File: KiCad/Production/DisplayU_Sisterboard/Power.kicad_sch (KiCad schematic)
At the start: 31 parts

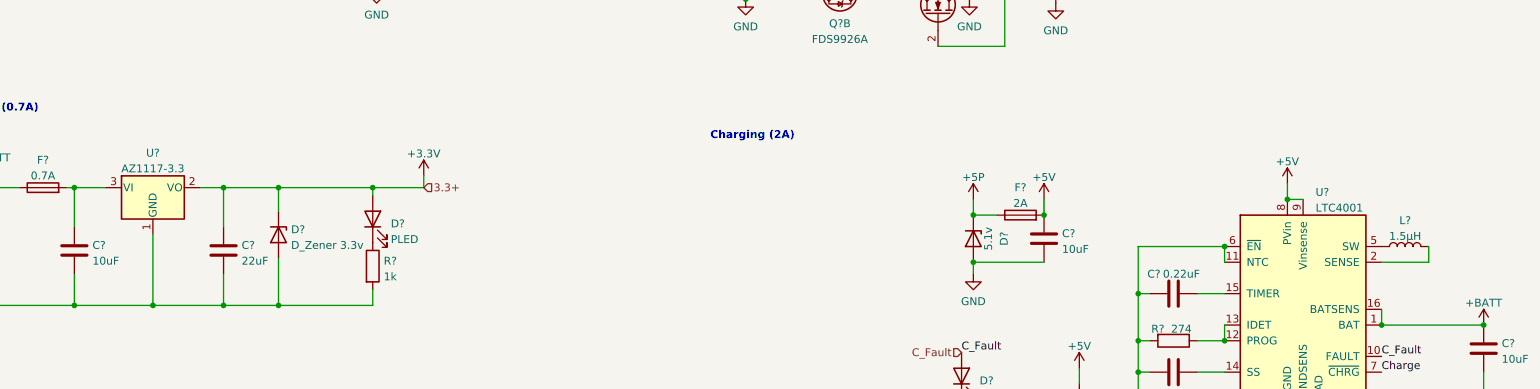
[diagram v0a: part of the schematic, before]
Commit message: Microcontroller Choice
Nordic nRF52820
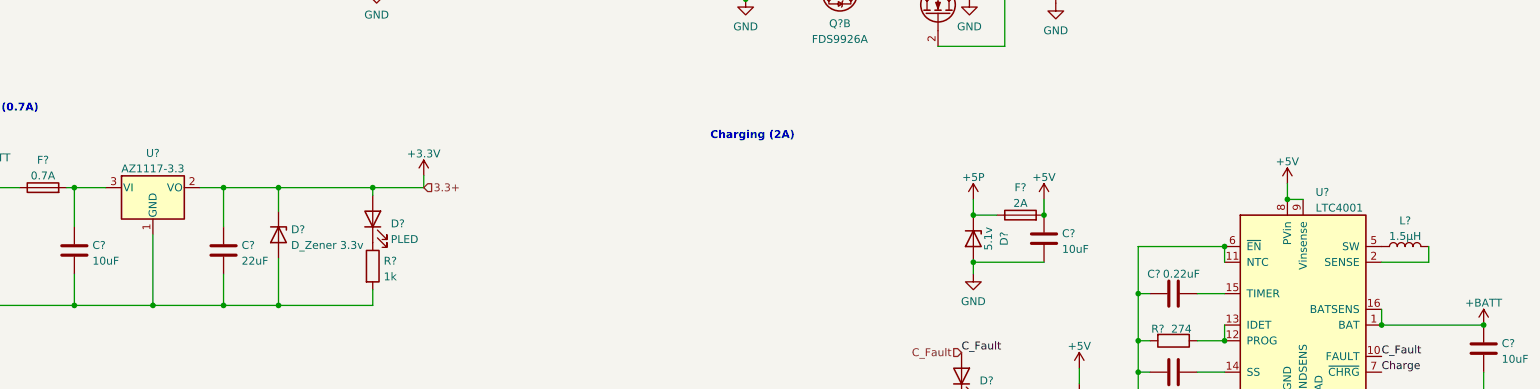
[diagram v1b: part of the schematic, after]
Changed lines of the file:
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@@
       (project "DisplayU_Sisterboard"
         (path "/19c7c935-33c8-4c59-9a5d-d605e15c31a3/bc90aa39-2744-4a84-88b0-6b5f6472e99d"
-          (reference "U6") (unit 1)
+          (reference "U4") (unit 1)
         )
       )
@@
       (project "DisplayU_Sisterboard"
         (path "/19c7c935-33c8-4c59-9a5d-d605e15c31a3/bc90aa39-2744-4a84-88b0-6b5f6472e99d"
-          (reference "U5") (unit 1)
+          (reference "U3") (unit 1)
         )
       )
@@
   (symbol (lib_id "Device:L") (at 265.43 118.745 90) (unit 1)
     (in_bom yes) (on_board yes) (dnp no) (fields_autoplaced)
-    (property "Reference" "L?" (at 265.43 114.5372 90)
-      (effects (font (size 1.27 1.27)))
-    )
-    (property "Value" "1.5µH" (at 265.43 117.0741 90)
+    (property "Reference" "L?" (at 265.43 114.5754 90)
+      (effects (font (size 1.27 1.27)))
+    )
+    (property "Value" "1.5µH" (at 265.43 117.0806 90)
       (effects (font (size 1.27 1.27)))
     )
@@
       (project "DisplayU_Sisterboard"
         (path "/19c7c935-33c8-4c59-9a5d-d605e15c31a3/bc90aa39-2744-4a84-88b0-6b5f6472e99d"
-          (reference "L2") (unit 1)
+          (reference "L5") (unit 1)
         )
       )
@@
   (symbol (lib_id "Regulator_Linear:AZ1117-3.3") (at 62.865 109.22 0) (unit 1)
     (in_bom yes) (on_board yes) (dnp no) (fields_autoplaced)
-    (property "Reference" "U?" (at 62.865 103.6152 0)
-      (effects (font (size 1.27 1.27)))
-    )
-    (property "Value" "AZ1117-3.3" (at 62.865 106.1521 0)
+    (property "Reference" "U?" (at 62.865 103.6508 0)
+      (effects (font (size 1.27 1.27)))
+    )
+    (property "Value" "AZ1117-3.3" (at 62.865 106.156 0)
       (effects (font (size 1.27 1.27)))
     )
@@
       (project "DisplayU_Sisterboard"
         (path "/19c7c935-33c8-4c59-9a5d-d605e15c31a3/bc90aa39-2744-4a84-88b0-6b5f6472e99d"
-          (reference "U4") (unit 1)
-        )
-      )
+          (reference "U2") (unit 1)
+        )
+      )

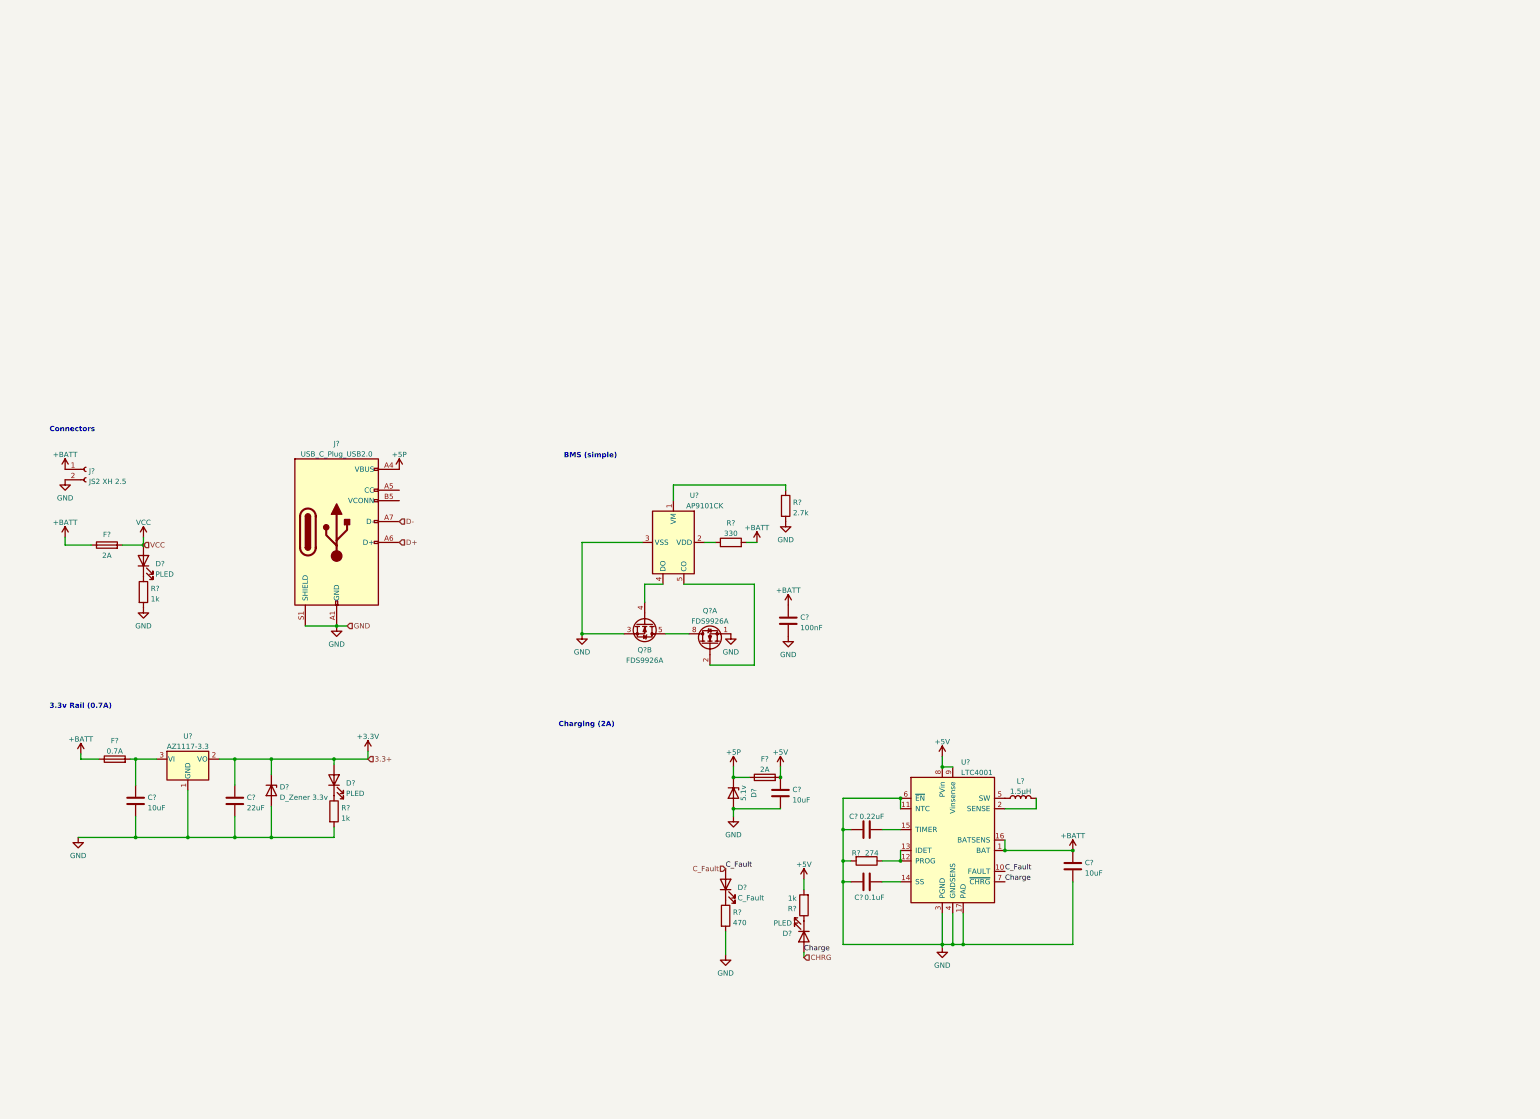
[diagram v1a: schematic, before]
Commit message: Display U is like 99% finished
- BMS Chips prob not needed
- LDO Chip prob not needed
- Final touches
> Start on routing
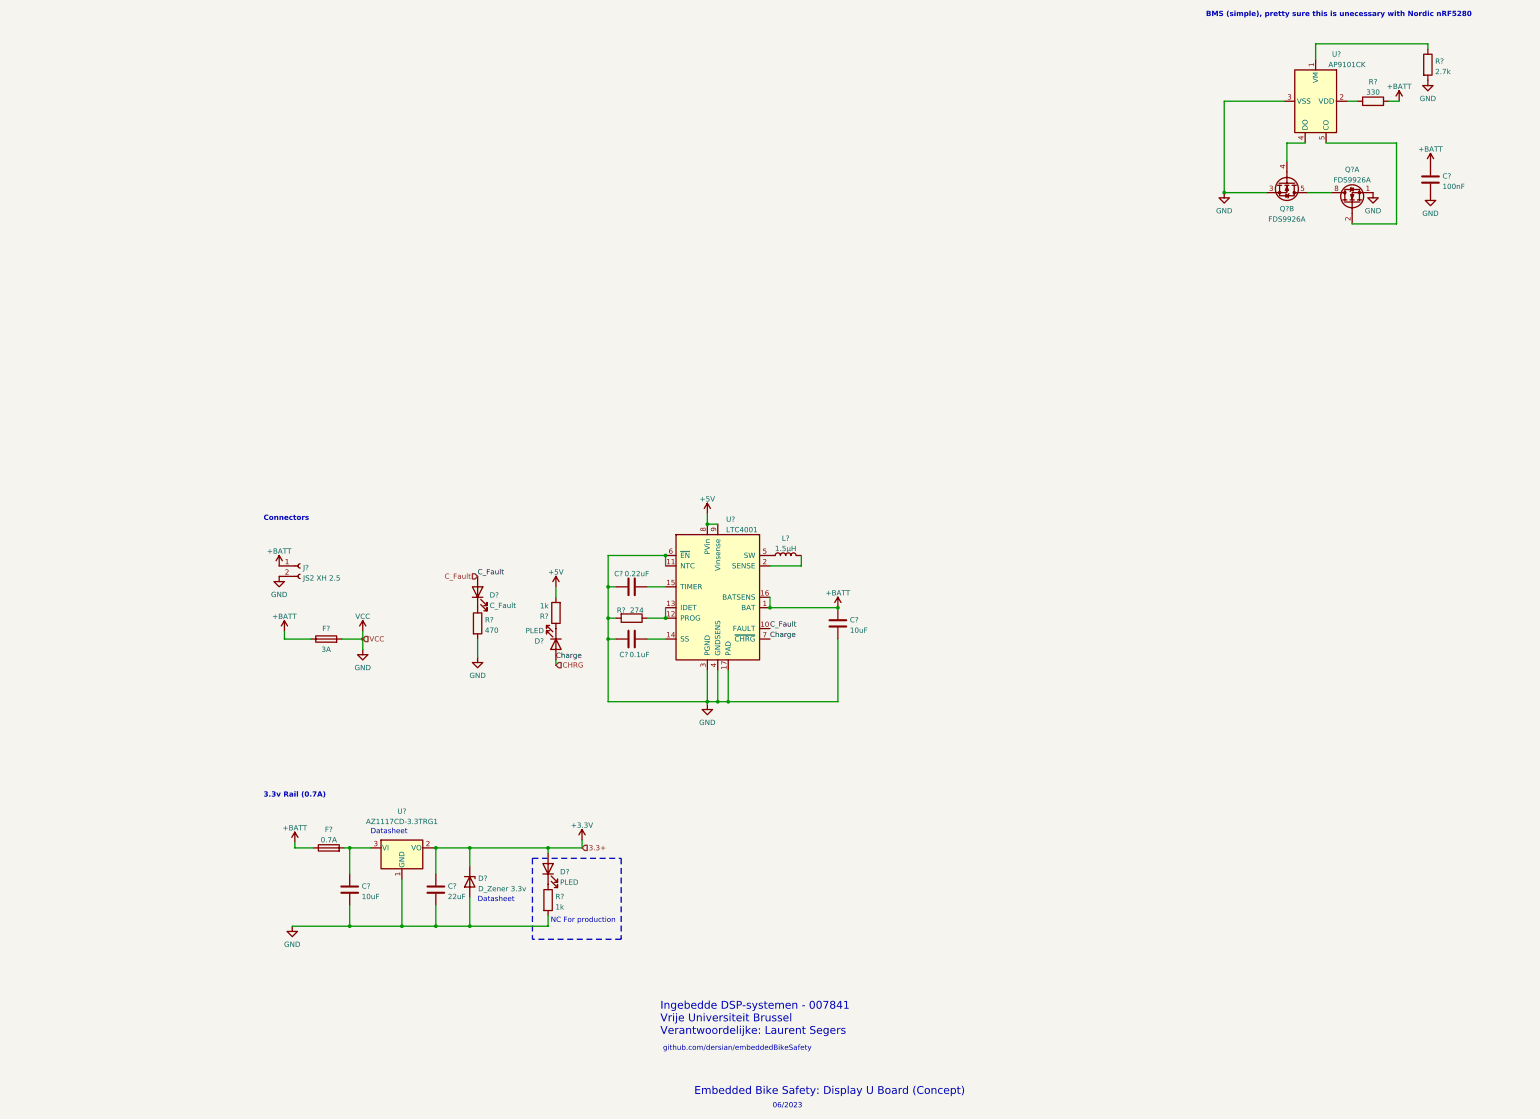
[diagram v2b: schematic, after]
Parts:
- removed C?: 10uF, Capacitor_SMD:C_0603_1608Metric_Pad1.08x0.95mm_HandSolder, symbol Device:C
- removed D?: PLED, symbol Device:LED
- removed D?: 5.1v, symbol Device:D_Zener
- removed F?: 2A, symbol Device:Fuse
- removed J?: USB_C_Plug_USB2.0, symbol Connector:USB_C_Plug_USB2.0
- removed R?: 1k, symbol Device:R
- C?: footprint (none) -> Capacitor_SMD:C_0603_1608Metric
- F?: value 2A -> 3A
- R? (x6): footprint (none) -> Resistor_SMD:R_0603_1608Metric
- U?: value AZ1117-3.3 -> AZ1117CD-3.3TRG1
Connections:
- net VCC is gone; now on net GND: F?.2
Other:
- note added: "06/2023"
- note added: "BMS (simple), pretty sure this is unecessary with Nordic nRF5280"
- note added: "Datasheet"
- note added: "Embedded Bike Safety: Display U Board (Concept)"
- note added: "Ingebedde DSP-systemen - 007841 Vrije Universiteit Brussel Verantwoordelijke: Laurent Segers"
- note added: "NC For production"
- note added: "github.com/dersian/embeddedBikeSafety"
- note removed: "BMS (simple)"
- note removed: "Charging (2A)"
- moved on the sheet: C?, D?, F?, J?, L?, Q?A, Q?B, R?, U?

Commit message: Schematic is done
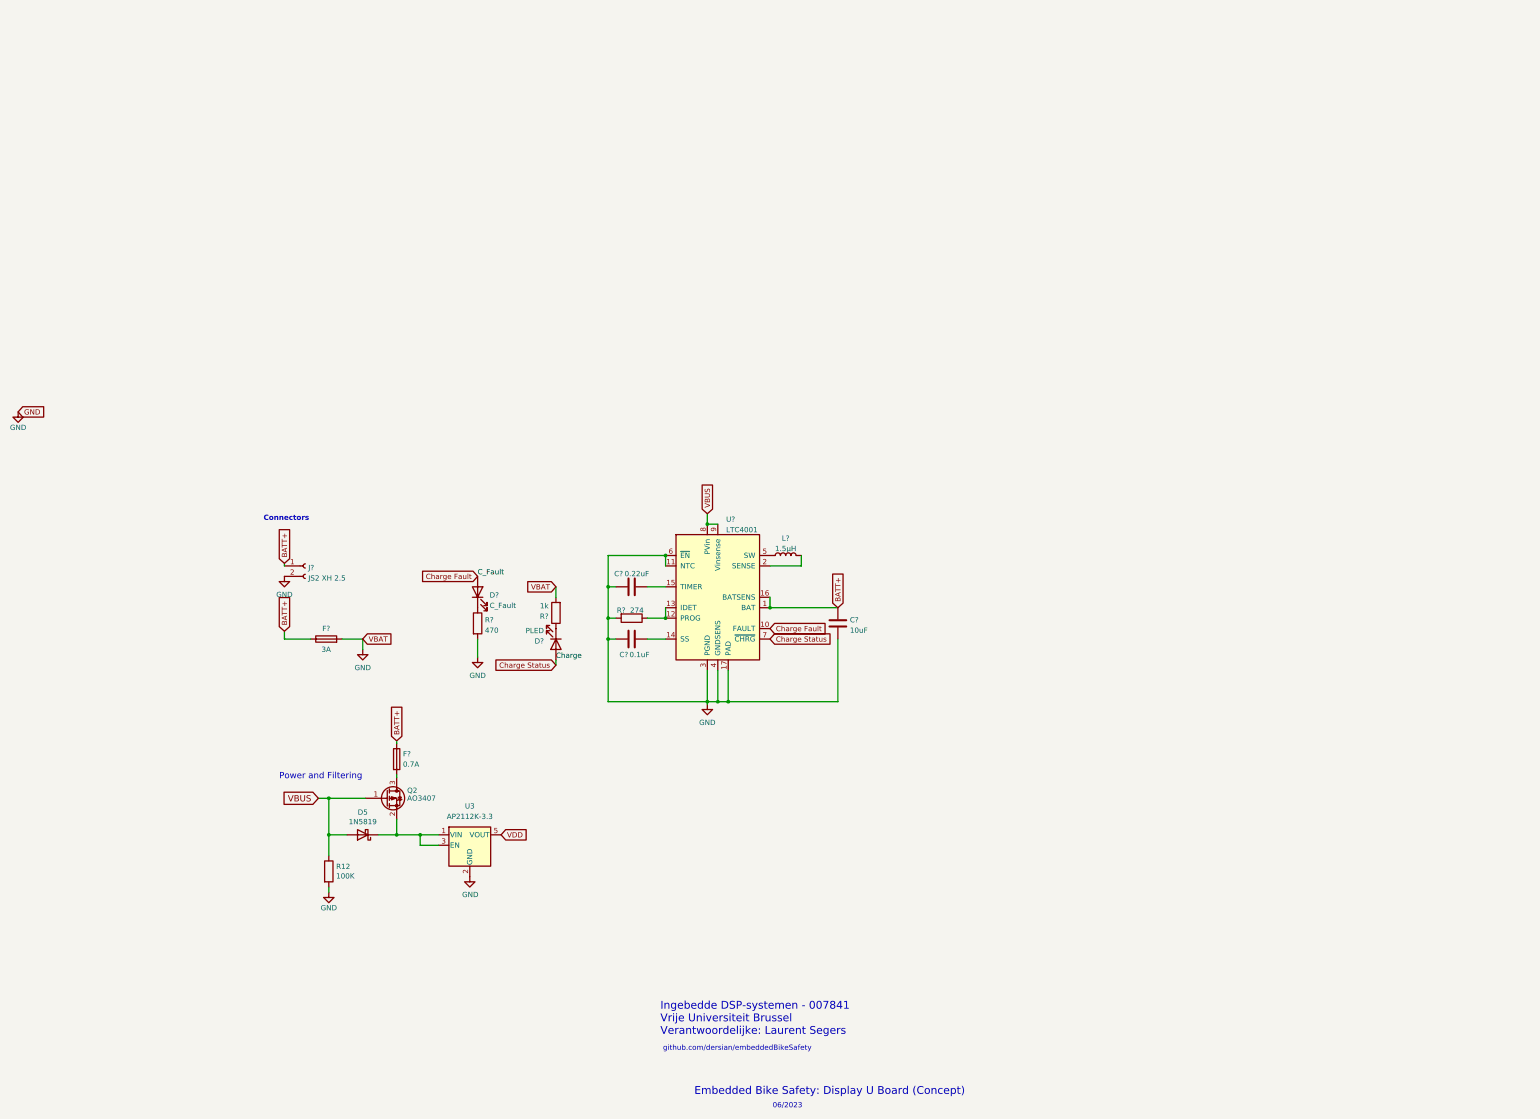
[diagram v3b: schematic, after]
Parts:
- removed C?: 100nF, Capacitor_SMD:C_0603_1608Metric_Pad1.08x0.95mm_HandSolder, symbol Device:C
- removed C?: 22uF, Capacitor_SMD:C_0603_1608Metric, symbol Device:C
- removed C?: 10uF, Capacitor_SMD:C_0603_1608Metric_Pad1.08x0.95mm_HandSolder, symbol Device:C
- removed D?: D_Zener 3.3v, symbol Device:D_Zener
- removed D?: PLED, symbol Device:LED
- removed F?: 0.7A, symbol Device:Fuse
- removed Q? (x2): FDS9926A, Package_SO:SOIC-8_3.9x4.9mm_P1.27mm, symbol Transistor_FET:FDS9926A
- removed R?: 2.7k, Resistor_SMD:R_0603_1608Metric, symbol Device:R
- removed R?: 330, Resistor_SMD:R_0603_1608Metric, symbol Device:R
- removed R?: 1k, Resistor_SMD:R_0603_1608Metric, symbol Device:R
- removed U?: AP9101CK, Package_TO_SOT_SMD:SOT-23-5, symbol Battery_Management:AP9101CK
- removed U?: AZ1117CD-3.3TRG1, symbol Regulator_Linear:AZ1117-3.3
- added D5: 1N5819, Diode_SMD:D_SOD-323F, symbol nrfmicro-rescue:MBR0520
- added F?: 0.7A, symbol Device:Fuse
- added Q2: AO3407, Package_TO_SOT_SMD:SOT-23, symbol nrfmicro-rescue:BSS83P
- added R12: 100K, Resistor_SMD:R_0603_1608Metric, symbol nrfmicro-rescue:R
- added U3: AP2112K-3.3, Package_TO_SOT_SMD:SOT-23-5, symbol Regulator_Linear:AP2112K-3.3
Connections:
- net GND: now also R?.2, R12.2, U3.2 (GND)
- net +5V renamed VBUS
- net VBUS: now also D5.2 (A), Q2.1 (G), R12.1; no longer R?.2
- net +BATT renamed BATT+
- net BATT+: now also F?.1
- net CHRG renamed Charge Status
- net C_Fault renamed Charge Fault
- new net: D5.1 (K), Q2.2 (S), U3.1 (VIN), U3.3 (EN)
- new net: F?.2, Q2.3 (D)
- new net VDD: U3.5 (VOUT)
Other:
- note added: "Power and Filtering"
- note removed: "3.3v Rail (0.7A)"
- note removed: "BMS (simple), pretty sure this is unecessary with Nordic nRF5280"
- note removed: "Datasheet"
- note removed: "NC For production"
- moved on the sheet: J?
